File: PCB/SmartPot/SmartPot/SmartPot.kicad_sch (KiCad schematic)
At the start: 8 parts, among them U1 TPS561208DDCT

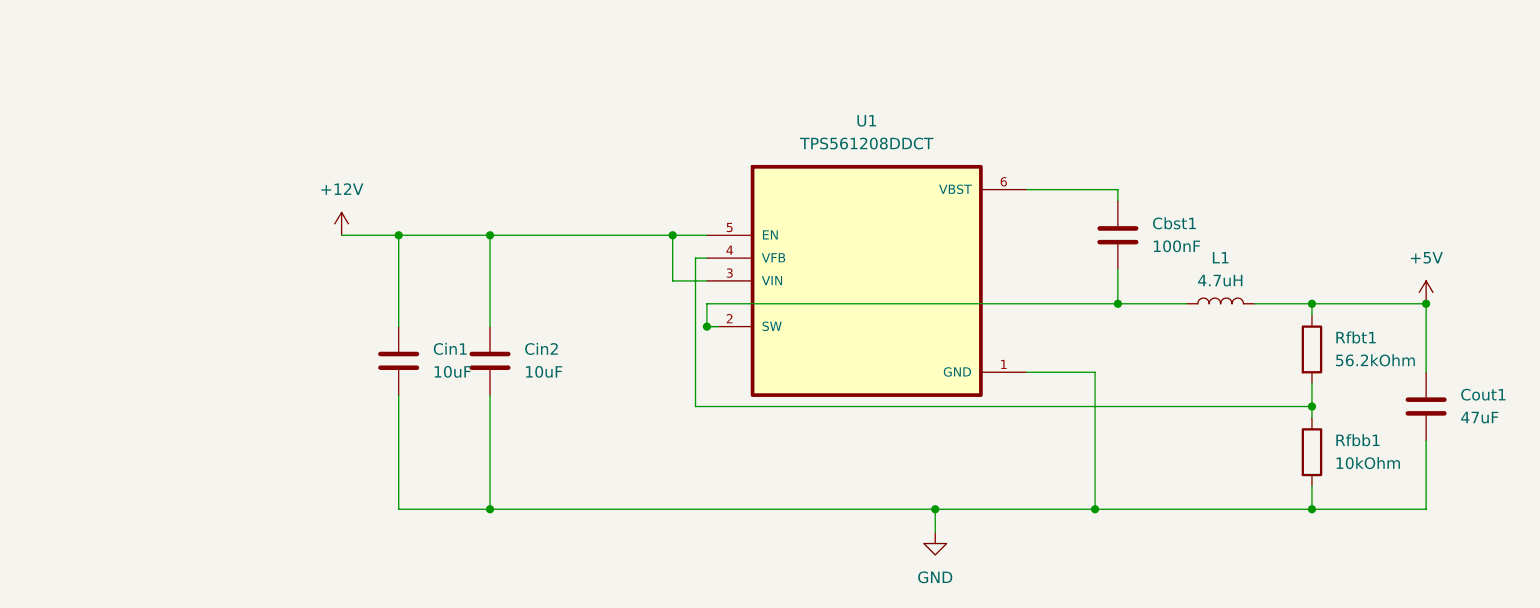
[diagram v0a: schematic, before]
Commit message: Added new components and modules
Signed-off-by: Simonca Raul <simonca.raul@gmail.com>
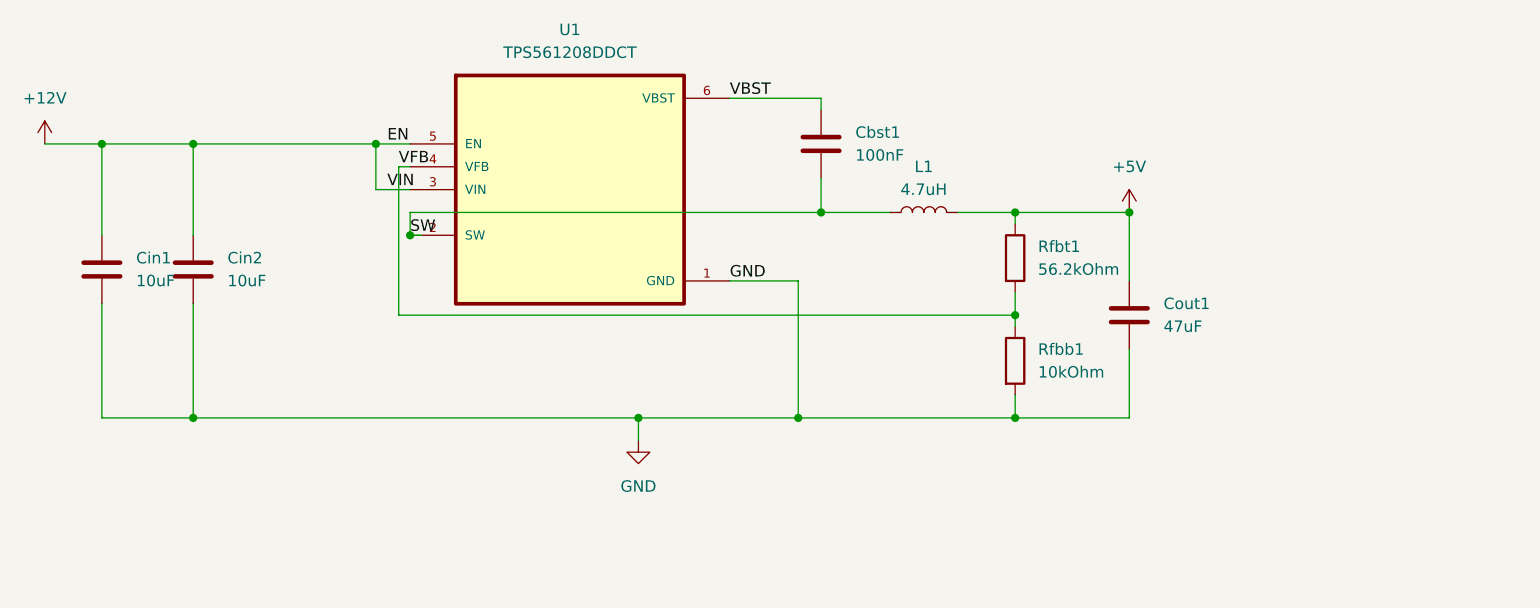
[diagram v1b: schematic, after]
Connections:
- net SW: now reaches Cbst1.2, L1.1, U1.2 (SW)
- net VFB: now reaches Rfbb1.1, Rfbt1.2, U1.4 (VFB)
- net VBST: now reaches Cbst1.1, U1.6 (VBST)
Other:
- moved on the sheet: Cbst1, Cin1, Cin2, Cout1, L1, Rfbb1, Rfbt1, U1

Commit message: Added switch modules and RS485 module
Signed-off-by: Simonca Raul <simonca.raul@gmail.com>
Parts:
- removed Cbst1: 100nF, Capacitor_SMD:C_1206_3216Metric_Pad1.33x1.80mm_HandSolder, symbol Device:C
- removed Cin1, Cin2: 10uF, Capacitor_SMD:C_1206_3216Metric_Pad1.33x1.80mm_HandSolder, symbol Device:C
- removed Cout1: 47uF, Capacitor_SMD:C_1206_3216Metric_Pad1.33x1.80mm_HandSolder, symbol Device:C
- removed L1: 4.7uH, Inductor_SMD:L_6.8x6.8_H3, symbol Device:L
- removed Rfbb1: 10kOhm, Resistor_SMD:R_1206_3216Metric, symbol Device:R
- removed Rfbt1: 56.2kOhm, Resistor_SMD:R_1206_3216Metric, symbol Device:R
- removed U1: TPS561208DDCT, Converter_DCDC:SOT95P280X110-6N, symbol Converter_DCDC:TPS561208DDCT

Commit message: Finalized the v4 of the PCB and added the web scraper test codes
Signed-off-by: Simonca Raul <simonca.raul@gmail.com>
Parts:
- added C1, C4: 100nF, Capacitor_SMD:C_1206_3216Metric, symbol Device:C
- added C2: 0.1uF, Capacitor_SMD:C_1206_3216Metric, symbol Device:C
- added C3: 10uF, Capacitor_SMD:C_1206_3216Metric, symbol Device:C
- added C5: 1uF, Capacitor_SMD:C_1206_3216Metric, symbol Device:C
- added Cbst1: 100nF, Capacitor_SMD:C_1206_3216Metric_Pad1.33x1.80mm_HandSolder, symbol Device:C
- added Cin1, Cin2: 10uF, Capacitor_SMD:C_1206_3216Metric_Pad1.33x1.80mm_HandSolder, symbol Device:C
- added Cout1: 47uF, Capacitor_SMD:C_1206_3216Metric_Pad1.33x1.80mm_HandSolder, symbol Device:C
- added D1: SM712_SOT23, Package_TO_SOT_SMD:SOT-23, symbol Diode:SM712_SOT23
- added D2: 1N4148W, Diode_SMD:D_SOD-123, symbol Diode:1N4148W
- added D3: LED, LED_THT:LED_D3.0mm_FlatTop, symbol Device:LED
- added F1: Fuse, Fuse:Fuse_1206_3216Metric, symbol Device:Fuse
- added J1, J2: Screw_Terminal_01x02, TerminalBlock:TerminalBlock_bornier-2_P5.08mm, symbol Connector:Screw_Terminal_01x02
- added J1: Screw_Terminal_01x04, TerminalBlock_Altech:Altech_AK100_1x04_P5.00mm, symbol Connector:Screw_Terminal_01x04
- added J3, J5: Conn_01x03_Pin, Connector_PinHeader_2.54mm:PinHeader_1x03_P2.54mm_Vertical, symbol Connector:Conn_01x03_Pin
- added J4: Barrel_Jack_MountingPin, Connector_BarrelJack:BarrelJack_Kycon_KLDX-0202-xC_Horizontal, symbol Connector:Barrel_Jack_MountingPin
- added J6: Conn_01x04_Pin, Connector_PinHeader_2.54mm:PinHeader_1x04_P2.54mm_Vertical, symbol Connector:Conn_01x04_Pin
- added J7, J8: Conn_01x02_Pin, Connector_PinHeader_2.54mm:PinHeader_1x02_P2.54mm_Vertical, symbol Connector:Conn_01x02_Pin
- added K1: AWHSH112DM00G, Relay_THT:AWHSH112DM00G, symbol Relay:AWHSH112DM00G
- added L1: 4.7uH, Inductor_SMD:L_6.8x6.8_H3, symbol Device:L
- added Q1: SSM3J352F_LF, Package_S-Mini:S-MINI_TOS, symbol Transistor_FET:SSM3J352F_LF
- added R1, R2, Rfbb1: 10kOhm, Resistor_SMD:R_1206_3216Metric, symbol Device:R
- added R10: 10kohm, Resistor_SMD:R_1206_3216Metric_Pad1.30x1.75mm_HandSolder, symbol Device:R
- added R11, R13: 56.2kOhm, Resistor_SMD:R_1206_3216Metric_Pad1.30x1.75mm_HandSolder, symbol Device:R
- added R12: 10kOhm, Resistor_SMD:R_1206_3216Metric_Pad1.30x1.75mm_HandSolder, symbol Device:R
- added R14, R15: 20kOhm, Resistor_SMD:R_1206_3216Metric_Pad1.30x1.75mm_HandSolder, symbol Device:R
- added R16: 250-400 Ohm, Resistor_SMD:R_1206_3216Metric, symbol Device:R
- added R3, R4: 10Ohm, Resistor_SMD:R_1210_3225Metric, symbol Device:R
- added R5: 120, Resistor_SMD:R_1206_3216Metric, symbol Device:R
- added R6, R7, R8, R9: R_Photo, OptoDevice:R_LDR_4.9x4.2mm_P2.54mm_Vertical, symbol Device:R_Photo
- added Rfbt1: 56.2kOhm, Resistor_SMD:R_1206_3216Metric, symbol Device:R
- added U1: THVD1400D, Package_SO:SOIC-8_3.9x4.9mm_P1.27mm, symbol Interface_UART:THVD1400D
- added U1: TPS561208DDCT, Converter_DCDC:SOT95P280X110-6N, symbol Converter_DCDC:TPS561208DDCT
- added U2: ADC084S021CIMM/NOPB, Package_SO:VSSOP-10_3x3mm_P0.5mm, symbol Analog_ADC:ADC084S021CIMM_NOPB
- added U3: ULN2003A, Package_SO:SOIC-16W_5.3x10.2mm_P1.27mm, symbol Transistor_Array:ULN2003A
- added U5: AVR32DA32x-xPT, Package_QFP:TQFP-32_7x7mm_P0.8mm, symbol MCU_Microchip_AVR_Dx:AVR32DA32x-xPT
- added U6: SHT31A-DIS, Sensor_Humidity:Sensirion_DFN-8-1EP_2.5x2.5mm_P0.5mm_EP1.1x1.7mm, symbol Sensor_Humidity:SHT31A-DIS
- added U7: ~, Modules:SHT31-Module, symbol Modules:SHT31-Module
- added U8: ~, Modules:HC12-Modules, symbol Modules:HC12-Module
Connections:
- new net: D3.1 (K), R16.1
- new net: F1.2, J4.1
- new net !SS: J6.4 (Pin_4), U2.1 (~CS), U5.5 (PA7)
- new net +12V: Cin1.1, Cin2.1, F1.1, J1.3 (Pin_3), K1.COM, Q1.2, Rfbb1.1, Rfbt1.2, U1.3 (VIN), U1.4 (VFB), U1.5 (EN), U3.9 (COM)
- new net +5V: C1.1, C2.1, C3.1, C4.1, C5.1, Cout1.1, J5.1 (Pin_1), L1.1, R1.1, R10.1, R11.1, R12.1, R13.1, R14.1, R15.1, Rfbt1.1, U1.8 (VCC), U2.2 (VA), U5.28 (VDD), U6.5 (VDD), U7.1 (VCC), U8.1 (VCC)
- new net A: D1.2 (A2), J1.2 (Pin_2), R3.2, R5.1
- new net Aout: R4.1, U1.7 (B)
- new net B: D1.1 (A1), J1.1 (Pin_1), R4.2, R5.2
- new net Bout: R3.1, U1.6 (A)
- new net COMM1: U3.1 (I1), U3.2 (I2), U5.31 (PA1)
- new net COMM2: U3.3 (I3), U5.30 (PA0)
- new net GND: C1.2, C2.2, C3.2, C4.2, C5.2, Cin1.2, Cin2.2, Cout1.2, D1.3 (common), D2.2 (A), J1.2 (Pin_2), J1.4 (Pin_4), J2.2 (Pin_2), J4.2, J5.2 (Pin_2), K1.V-, R16.2, R2.2, R6.2, R7.2, R8.2, R9.2, Rfbb1.2, U1.1 (GND), U1.5 (GND), U2.3 (GND), U3.8 (GND), U5.19 (GND), U5.29 (GND), U6.2 (ADDR), U6.7 (R), U6.8 (VSS), U6.9 (VSS), U7.2 (GND), U8.2 (GND)
- new net IN1: R10.2, R6.1, U2.7 (IN1)
- new net IN2: R13.2, R7.1, U2.6 (IN2)
- new net IN3: R11.2, R8.1, U2.5 (IN3)
- new net IN4: R12.2, R9.1, U2.4 (IN4)
- new net LOAD: J1.1 (Pin_1), Q1.3
- new net MCLED: D3.2 (A), U5.25 (PF5)
- new net MISO0: J6.2 (Pin_2), U2.9 (DOUT), U5.3 (PA5)
- new net MOSI0: J6.1 (Pin_1), U2.8 (DIN), U5.2 (PA4)
- new net OPEN: J2.1 (Pin_1), K1.OPEN
- new net OUT1: D2.1 (K), K1.V+, U3.15 (O2), U3.16 (O1)
- new net OUT2: Q1.1, U3.14 (O3)
- new net RX1: J3.2 (Pin_2), R1.2, U1.1 (RO), U5.7 (PC1)
- new net RX2: U5.21 (XTAL32K2/PF1), U8.4 (TX)
- new net SCK: J6.3 (Pin_3), U2.10 (SCLK), U5.4 (PA6)
- new net SCL0: J7.2 (Pin_2), U5.1 (PA3), U7.3 (SCL)
- new net SCL1: J8.1 (Pin_1), R15.2, U5.23 (PF3), U6.4 (SCL)
- new net SDA0: J7.1 (Pin_1), U5.32 (PA2), U7.4 (SDA)
- new net SDA1: J8.2 (Pin_2), R14.2, U5.22 (PF2), U6.1 (SDA)
- new net SET: U5.24 (PF4), U8.5 (SET)
- new net SW: Cbst1.2, L1.2, U1.2 (SW)
- new net TX1: J3.1 (Pin_1), U1.4 (DI), U5.6 (PC0)
- new net TX2: U5.20 (XTAL32K1/PF0), U8.3 (RX)
- new net UPDI: J5.3 (Pin_3), U5.27 (UPDI)
- new net VBST: Cbst1.1, U1.6 (VBST)
- new net XDIR1: J3.3 (Pin_3), R2.1, U1.2 (~{RE}), U1.3 (DE), U5.9 (PC3)
- no-connect marks 0 -> 22
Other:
- note added: "NEEDS A ULN2003AD TO DRIVE IT"

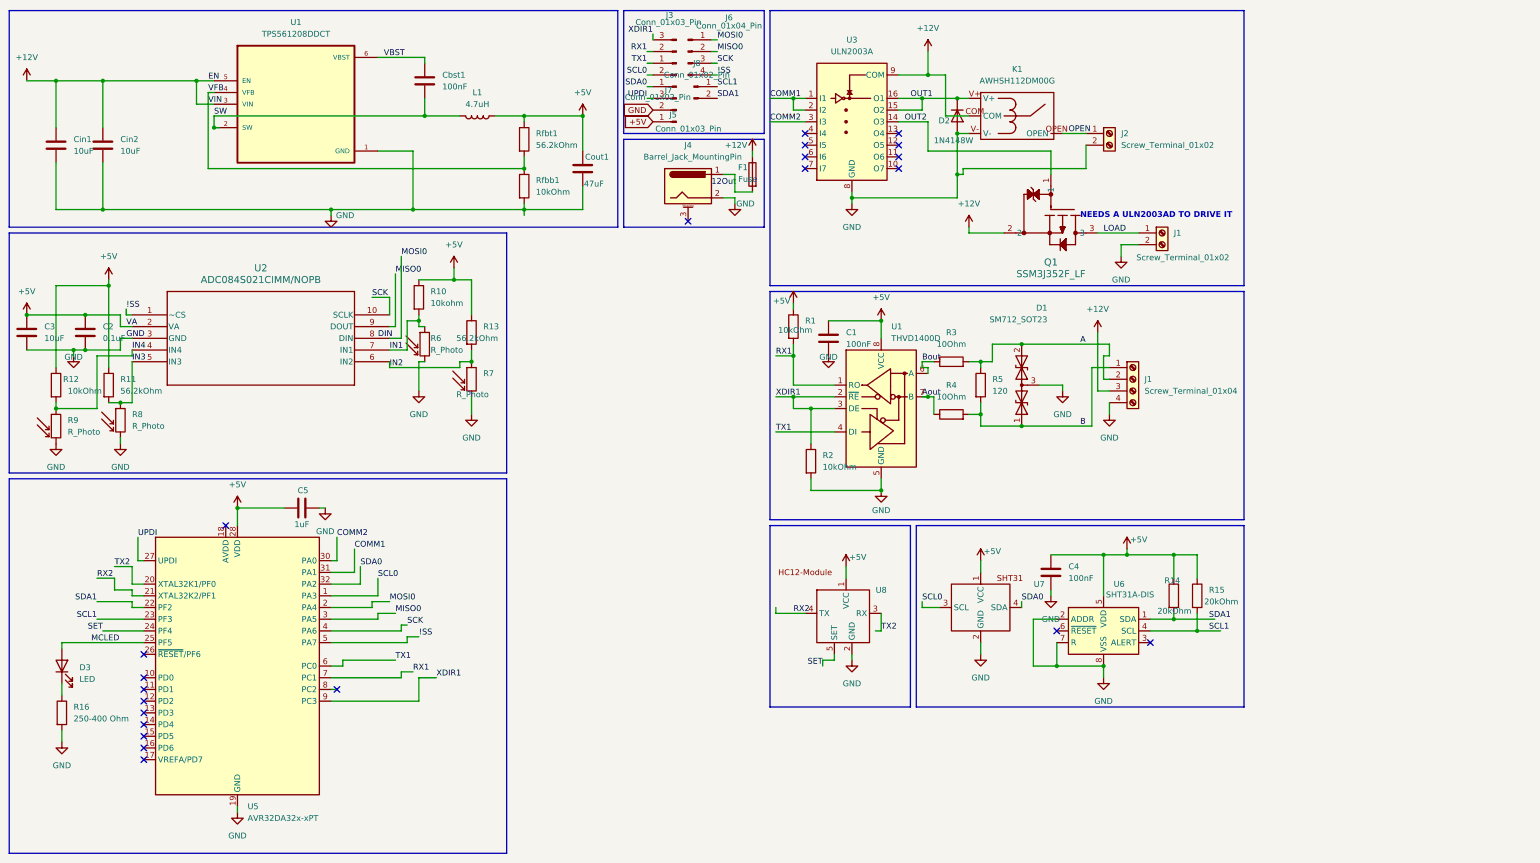
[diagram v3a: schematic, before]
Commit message: Added code fro rasp zero and updated the PCB
Signed-off-by: Simonca Raul <simonca.raul@gmail.com>
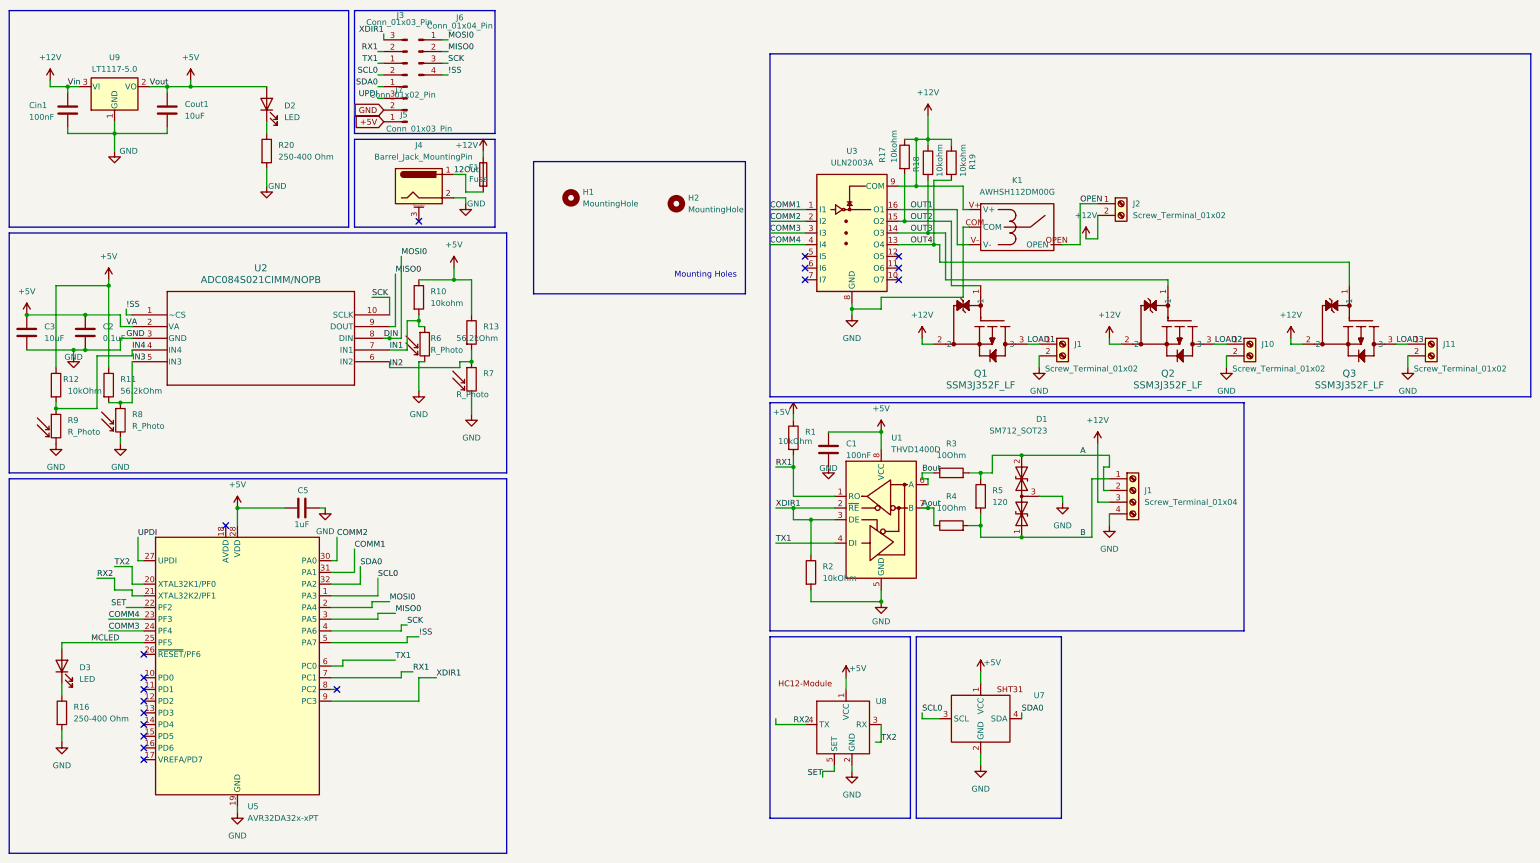
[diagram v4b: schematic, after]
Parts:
- removed C4: 100nF, Capacitor_SMD:C_1206_3216Metric, symbol Device:C
- removed Cin2: 10uF, Capacitor_SMD:C_1206_3216Metric_Pad1.33x1.80mm_HandSolder, symbol Device:C
- removed Cout1: 47uF, Capacitor_SMD:C_1206_3216Metric_Pad1.33x1.80mm_HandSolder, symbol Device:C
- removed D2: 1N4148W, Diode_SMD:D_SOD-123, symbol Diode:1N4148W
- removed J8: Conn_01x02_Pin, Connector_PinHeader_2.54mm:PinHeader_1x02_P2.54mm_Vertical, symbol Connector:Conn_01x02_Pin
- removed L1: 4.7uH, Inductor_SMD:L_6.8x6.8_H3, symbol Device:L
- removed R14, R15: 20kOhm, Resistor_SMD:R_1206_3216Metric_Pad1.30x1.75mm_HandSolder, symbol Device:R
- removed Rfbb1: 10kOhm, Resistor_SMD:R_1206_3216Metric, symbol Device:R
- removed Rfbt1: 56.2kOhm, Resistor_SMD:R_1206_3216Metric, symbol Device:R
- removed U1: TPS561208DDCT, Converter_DCDC:SOT95P280X110-6N, symbol Converter_DCDC:TPS561208DDCT
- removed U6: SHT31A-DIS, Sensor_Humidity:Sensirion_DFN-8-1EP_2.5x2.5mm_P0.5mm_EP1.1x1.7mm, symbol Sensor_Humidity:SHT31A-DIS
- added D2: LED, LED_THT:LED_D3.0mm_FlatTop, symbol Device:LED
- added H1, H2: MountingHole, MountingHole:MountingHole_3.5mm, symbol Mechanical:MountingHole
- added J10, J11: Screw_Terminal_01x02, TerminalBlock:TerminalBlock_bornier-2_P5.08mm, symbol Connector:Screw_Terminal_01x02
- added Q2, Q3: SSM3J352F_LF, Package_S-Mini:S-MINI_TOS, symbol Transistor_FET:SSM3J352F_LF
- added R17, R18, R19: 10kohm, Resistor_SMD:R_1206_3216Metric_Pad1.30x1.75mm_HandSolder, symbol Device:R
- added R20: 250-400 Ohm, Resistor_SMD:R_1206_3216Metric, symbol Device:R
- added U9: LT1117-5.0, Package_TO_SOT_SMD:SOT-223-3_TabPin2, symbol Regulator_Linear:LT1117-5.0
- renumbered Cbst1 to Cin1, Cin1 to Cout1
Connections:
- net MOSI0 is gone; now on net DIN: J6.1 (Pin_1), U2.8 (DIN), U5.2 (PA4)
- net SCL1 is gone; now on net COMM4: U5.23 (PF3)
- net SDA1 is gone; now on net SET: U5.22 (PF2)
- net SW is gone; now on net GND: Cin1.2
- net VBST is gone; now on net +12V: Cin1.1
- net +12V: now also J2.2 (Pin_2), K1.V+, Q2.2, Q3.2, R17.1, R18.1, R19.1, U9.3 (VI); no longer Cout1.1, K1.COM
- net +5V: now also Cout1.1, D2.2 (A), U9.2 (VO)
- net 12Out: now also F1.2, J4.1
- net COMM1: no longer U3.2 (I2)
- net COMM2: now also U3.2 (I2); no longer U3.3 (I3)
- net GND: now also K1.COM, J10.2 (Pin_2), J11.2 (Pin_2), R20.2, U9.1 (GND); no longer J2.2 (Pin_2), K1.V-
- net OUT1: now also K1.V-; no longer K1.V+, U3.15 (O2)
- net OUT2: now also U3.15 (O2), R17.2; no longer U3.14 (O3)
- net SET: no longer U5.24 (PF4)
- net OUT4: now reaches U3.13 (O4)
- net OUT4: now also Q3.1, R19.2
- net COMM4: now reaches U3.4 (I4)
- net LOAD renamed LOAD1
- new net: D2.1 (K), R20.1
- new net COMM3: U3.3 (I3), U5.24 (PF4)
- new net LOAD2: J10.1 (Pin_1), Q2.3
- new net LOAD3: J11.1 (Pin_1), Q3.3
- new net OUT3: Q2.1, R18.2, U3.14 (O3)
- no-connect marks 22 -> 18
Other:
- note added: "Mounting Holes"
- note removed: "NEEDS A ULN2003AD TO DRIVE IT"
- moved on the sheet: C1, Cin1, Cout1, D1, F1, J1, J2, J3, J4, J5, J6, J7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
